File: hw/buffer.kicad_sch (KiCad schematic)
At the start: 35 parts, among them J2001 BNC, J2002 RFShield_Front, J2003 RFShield_Back, K2001 G6L-1F, U2001 TS5A63157DCK, U2002 AQY280S, U2003 AD8370, U2004 OPA859xDSG

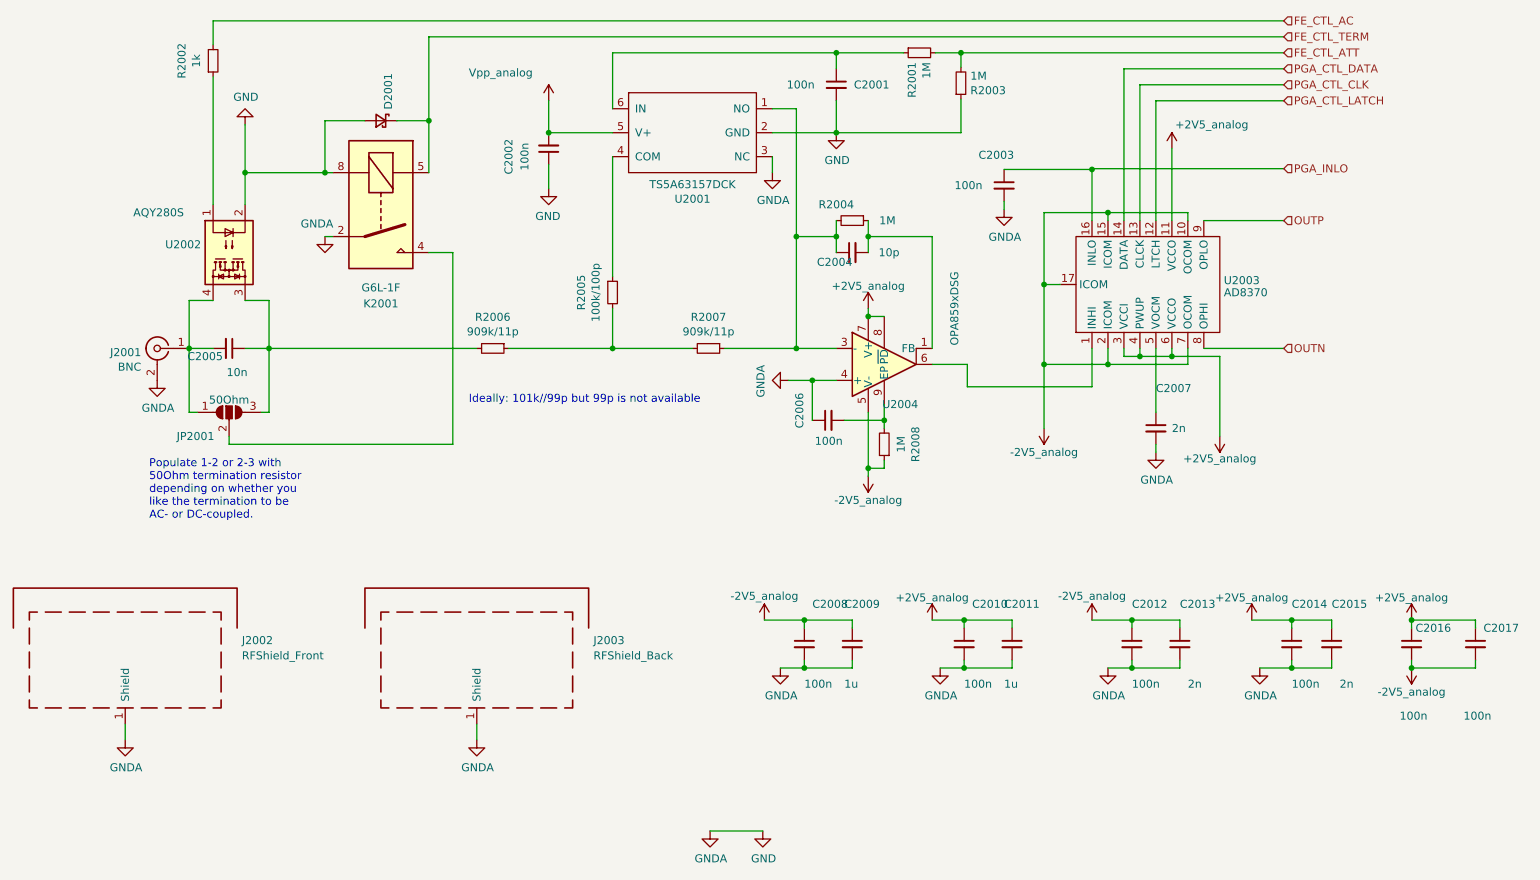
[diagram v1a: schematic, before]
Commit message: added pll clock in divider from BNC, several pull-resistors
pull-resistors permit distinguishing board revisions.
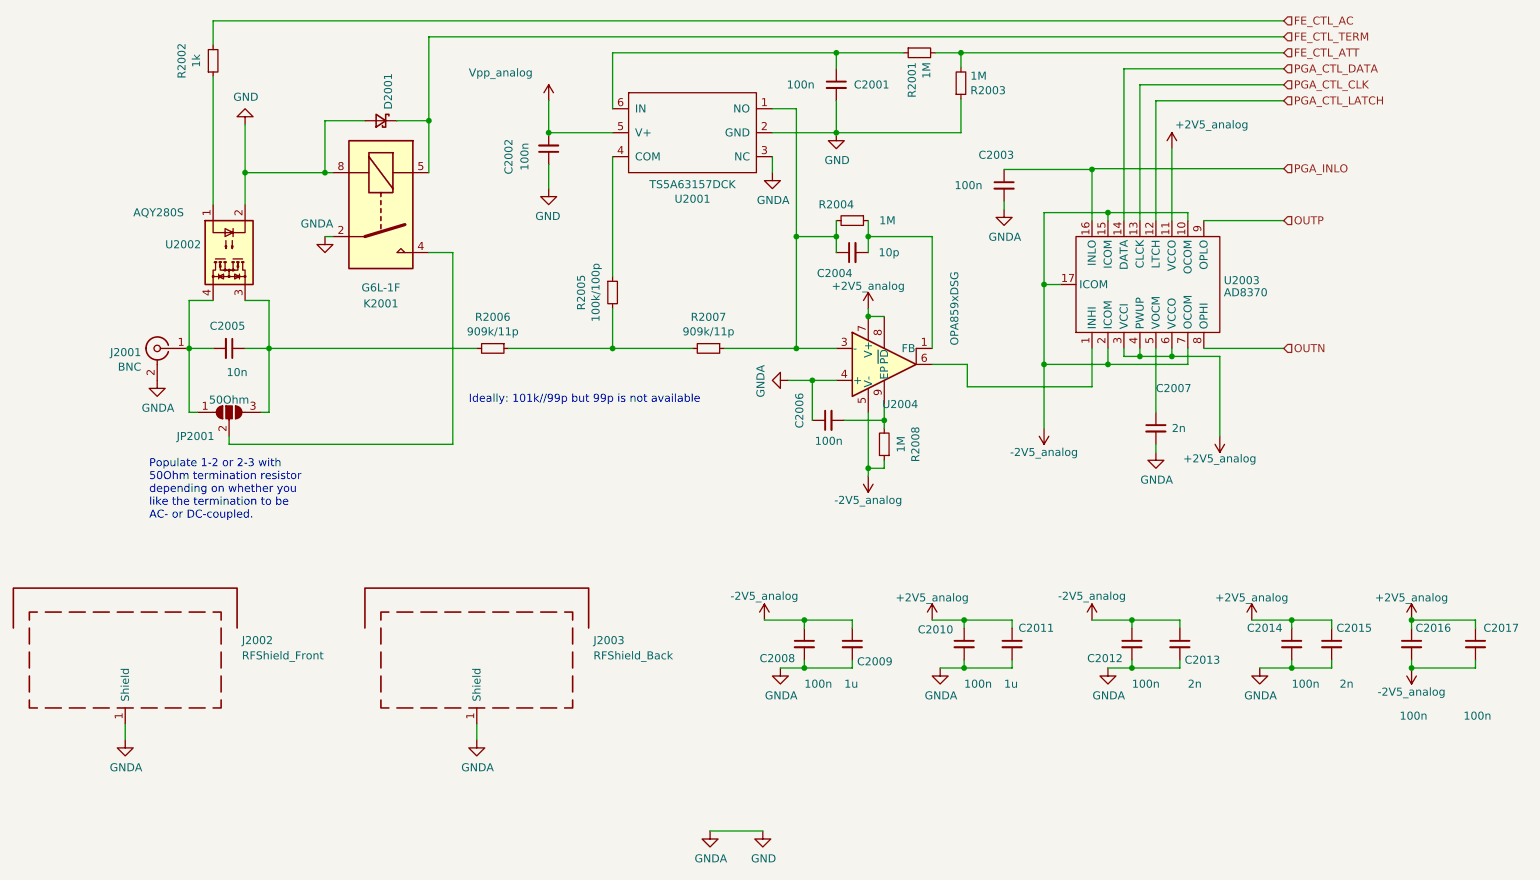
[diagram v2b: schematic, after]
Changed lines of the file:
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@@
 		(dnp no)
 		(property "Reference" "C2010"
-			(at 184.15 142.24 0)
+			(at 175.514 146.304 0)
 			(effects
 				(font
@@
 		(dnp no)
 		(property "Reference" "C2011"
-			(at 189.23 142.24 0)
+			(at 191.516 146.05 0)
 			(effects
 				(font
@@
 		(dnp no)
 		(property "Reference" "C2008"
-			(at 158.75 142.24 0)
+			(at 150.368 150.876 0)
 			(effects
 				(font
@@
 		(dnp no)
 		(property "Reference" "C2009"
-			(at 163.83 142.24 0)
+			(at 165.862 151.384 0)
 			(effects
 				(font
@@
 		(dnp no)
 		(property "Reference" "C2004"
-			(at 162.306 87.884 90)
+			(at 162.306 89.662 90)
 			(effects
 				(font
@@
 		(dnp no)
 		(property "Reference" "C2013"
-			(at 217.17 142.24 0)
+			(at 217.932 151.13 0)
 			(effects
 				(font
@@
 		(dnp no)
 		(property "Reference" "C2015"
-			(at 241.3 142.24 0)
+			(at 242.062 146.05 0)
 			(effects
 				(font
@@
 		(dnp no)
 		(property "Reference" "C2005"
-			(at 62.23 102.87 90)
+			(at 65.786 98.044 90)
 			(effects
 				(font
@@
 		(dnp no)
 		(property "Reference" "C2014"
-			(at 234.95 142.24 0)
+			(at 227.838 146.05 0)
 			(effects
 				(font
@@
 		(dnp no)
 		(property "Reference" "C2012"
-			(at 209.55 142.24 0)
+			(at 202.438 150.876 0)
 			(effects
 				(font

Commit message: updated parts assignments
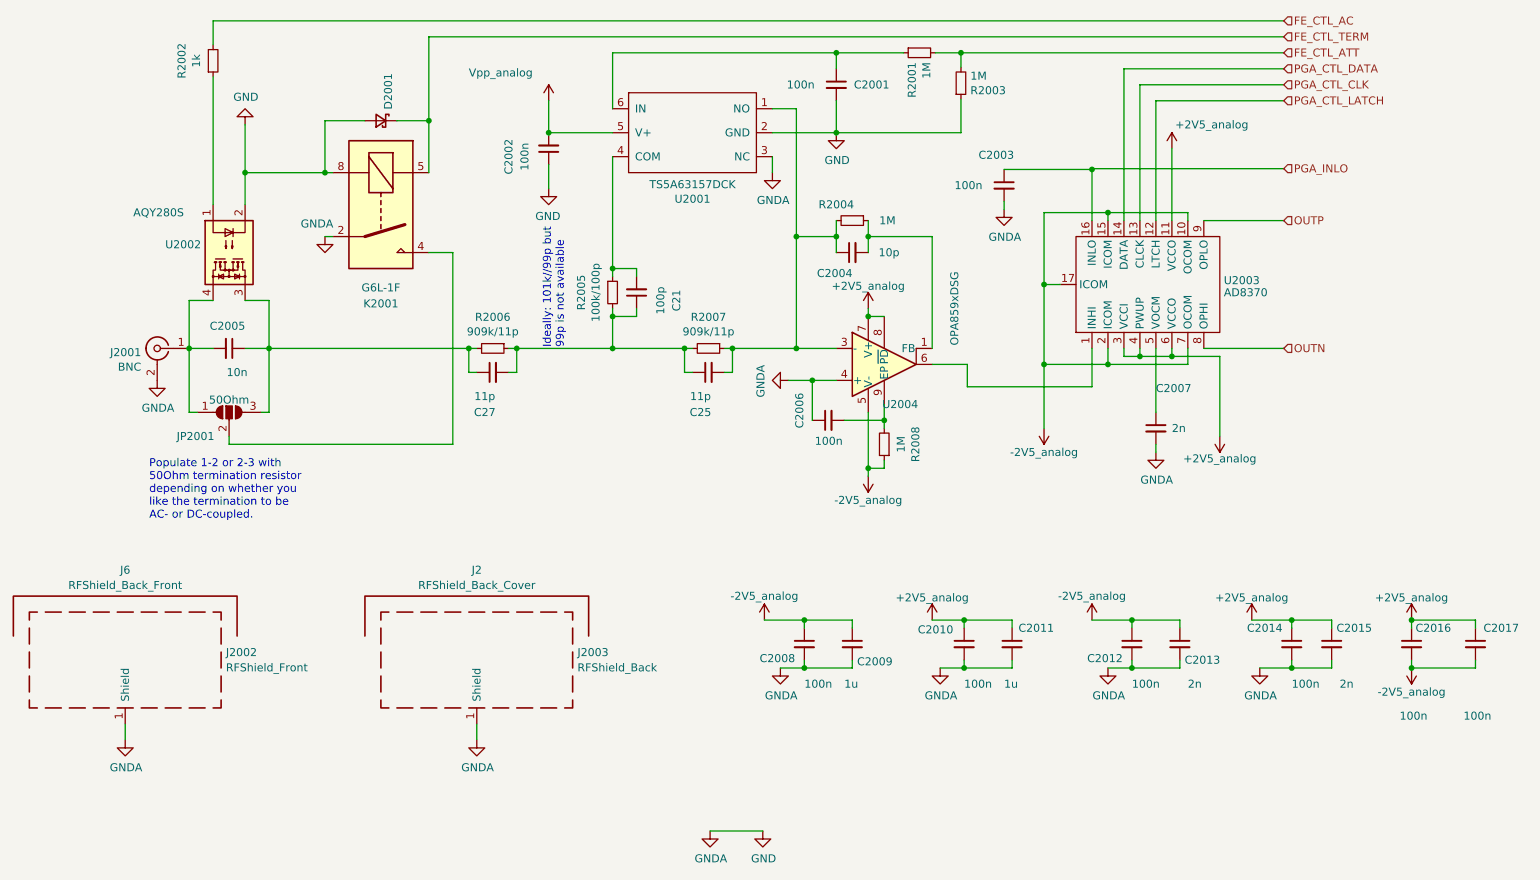
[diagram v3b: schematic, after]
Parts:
- added C21: 100p, Capacitor_SMD:C_0603_1608Metric, symbol Device:C_Small
- added C25, C27: 11p, Capacitor_SMD:C_0603_1608Metric, symbol Device:C_Small
- added J2: RFShield_Back_Cover, symbol fmc:RFShield_Cover
- added J6: RFShield_Back_Front, symbol fmc:RFShield_Cover
- C2004: Manufacturer (none) -> Murata; Part (none) -> GJM1555C1H100FB01D
- C2005: Manufacturer (none) -> Murata; Part (none) -> GRM21B5C2E103JWAAL
- C2007, C2013, C2015: Manufacturer (none) -> Yageo; Part (none) -> CC0603KRX7R9BB202
- J2002: symbol Device:RFShield_TwoPieces -> Device:RFShield_OnePiece; Part SMS-255F+C -> SMS-255F
- J2003: symbol Device:RFShield_TwoPieces -> Device:RFShield_OnePiece; Part SMS-202F+C -> SMS-202F
- JP2001: Manufacturer (none) -> Panasonic; Part (none) -> ERJ-PA3F49R9V
- R2001, R2003, R2008: Manufacturer (none) -> Stackpole; Part (none) -> RMCF0603FT1M00
- R2002: Manufacturer (none) -> Stackpole; Part (none) -> RMCF0603FT1K00
- R2004: Manufacturer (none) -> Stackpole; Part (none) -> RMCF0402FT1M00
- R2005: Manufacturer (none) -> Stackpole; Part (none) -> RMCF0603FT100K
- R2006, R2007: Manufacturer (none) -> Panasonic; Part (none) -> ERJ-3EKF9093V
- U2001: Manufacturer (none) -> TI; Part (none) -> TS5A63157DCKR
- U2002: Manufacturer (none) -> Panasonic; Part (none) -> AQY280S
- U2003: Manufacturer (none) -> AD; Part (none) -> AD8370AREZ
- U2004: Manufacturer (none) -> TI; Part (none) -> OPA859IDSGR
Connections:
- net at R2005.1, U2001.4 (COM): now also C21.2
- net at R2005.2, R2006.1, R2007.2: now also C21.1, C25.1, C27.2
- net at C2005.1, JP2001.3 (B), R2006.2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: now also C27.1
- net at C2004.1, R2004.2, R2007.1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: now also C25.2

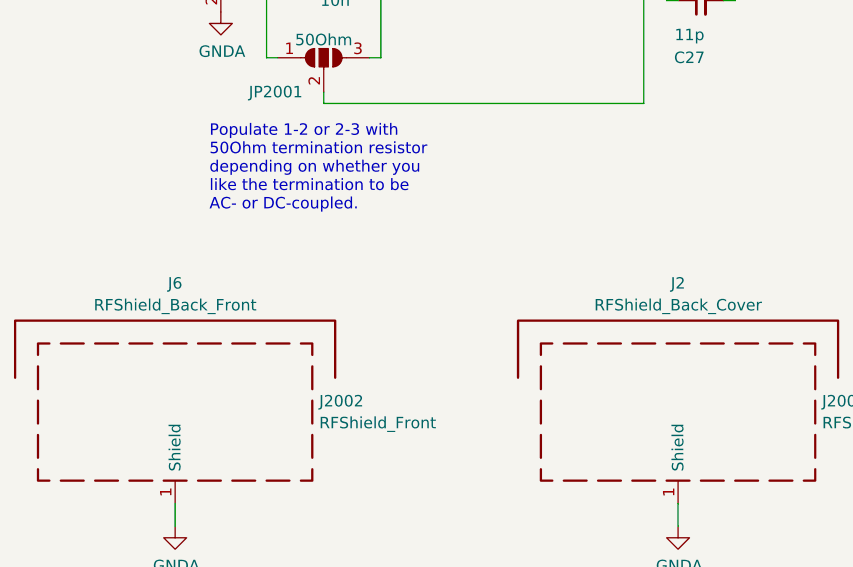
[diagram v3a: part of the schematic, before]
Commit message: fixed BOM; added relay drivers
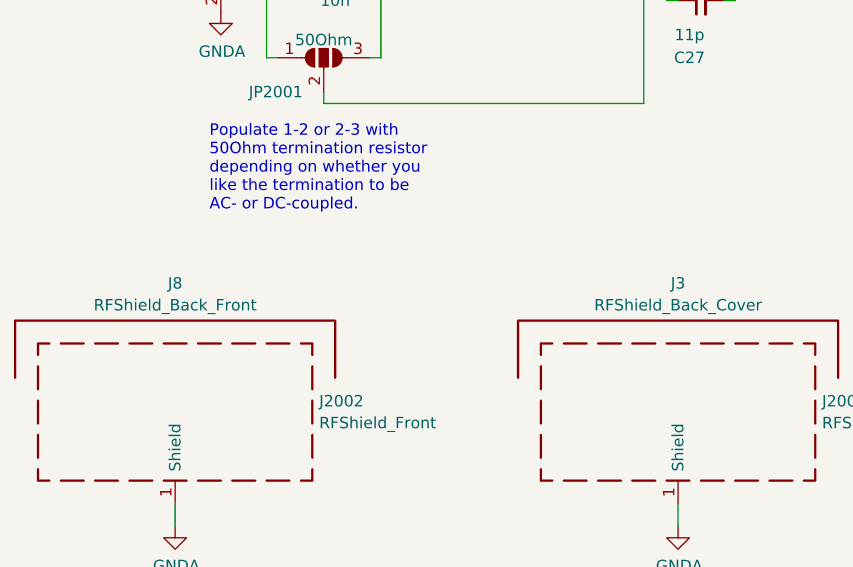
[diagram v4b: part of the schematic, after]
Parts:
- K2001: Part G6L-1F -> G6L-1F DC4.5
- renumbered J2 to J3, J6 to J8
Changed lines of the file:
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@@
 			)
 		)
-		(property "Part" "G6L-1F"
+		(property "Part" "G6L-1F DC4.5"
 			(at 90.17 78.74 90)
 			(effects
@@
 		(dnp no)
 		(fields_autoplaced yes)
-		(property "Reference" "J6"
+		(property "Reference" "J8"
 			(at 49.53 136.8255 0)
 			(effects
@@
 		(dnp no)
 		(fields_autoplaced yes)
-		(property "Reference" "J2"
+		(property "Reference" "J3"
 			(at 105.41 136.8255 0)
 			(effects

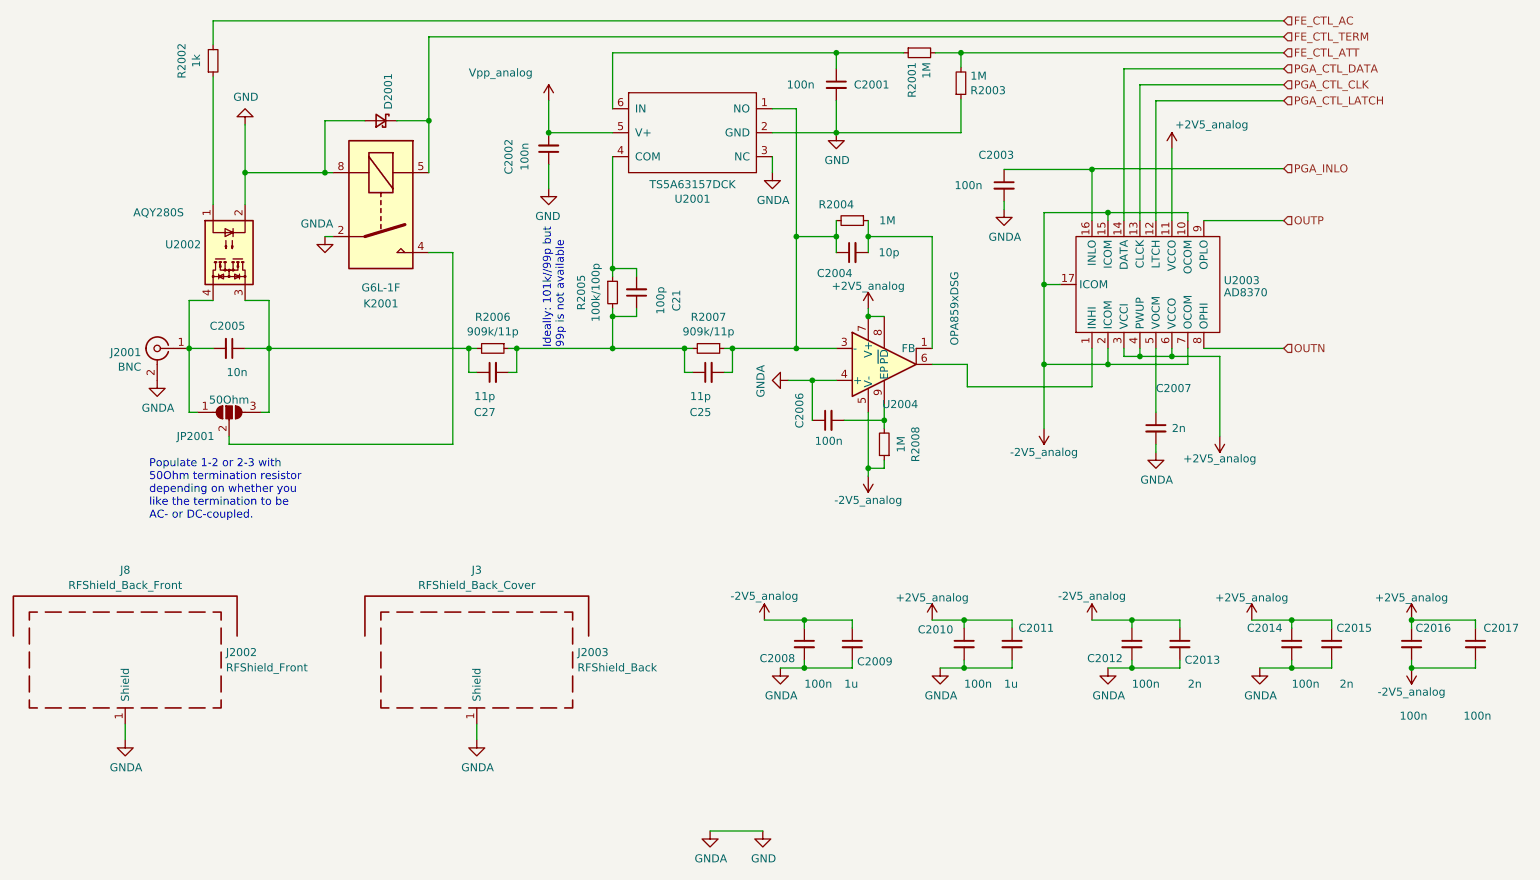
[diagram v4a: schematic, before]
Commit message: connected versaclock CLKSEL to ULPI RSTB (share FPGA pin)
ULPI Rstb is unlikely to be used

Also: - update of kicad to 9.0 (many library footprints updated)
      - added sheet titles, author
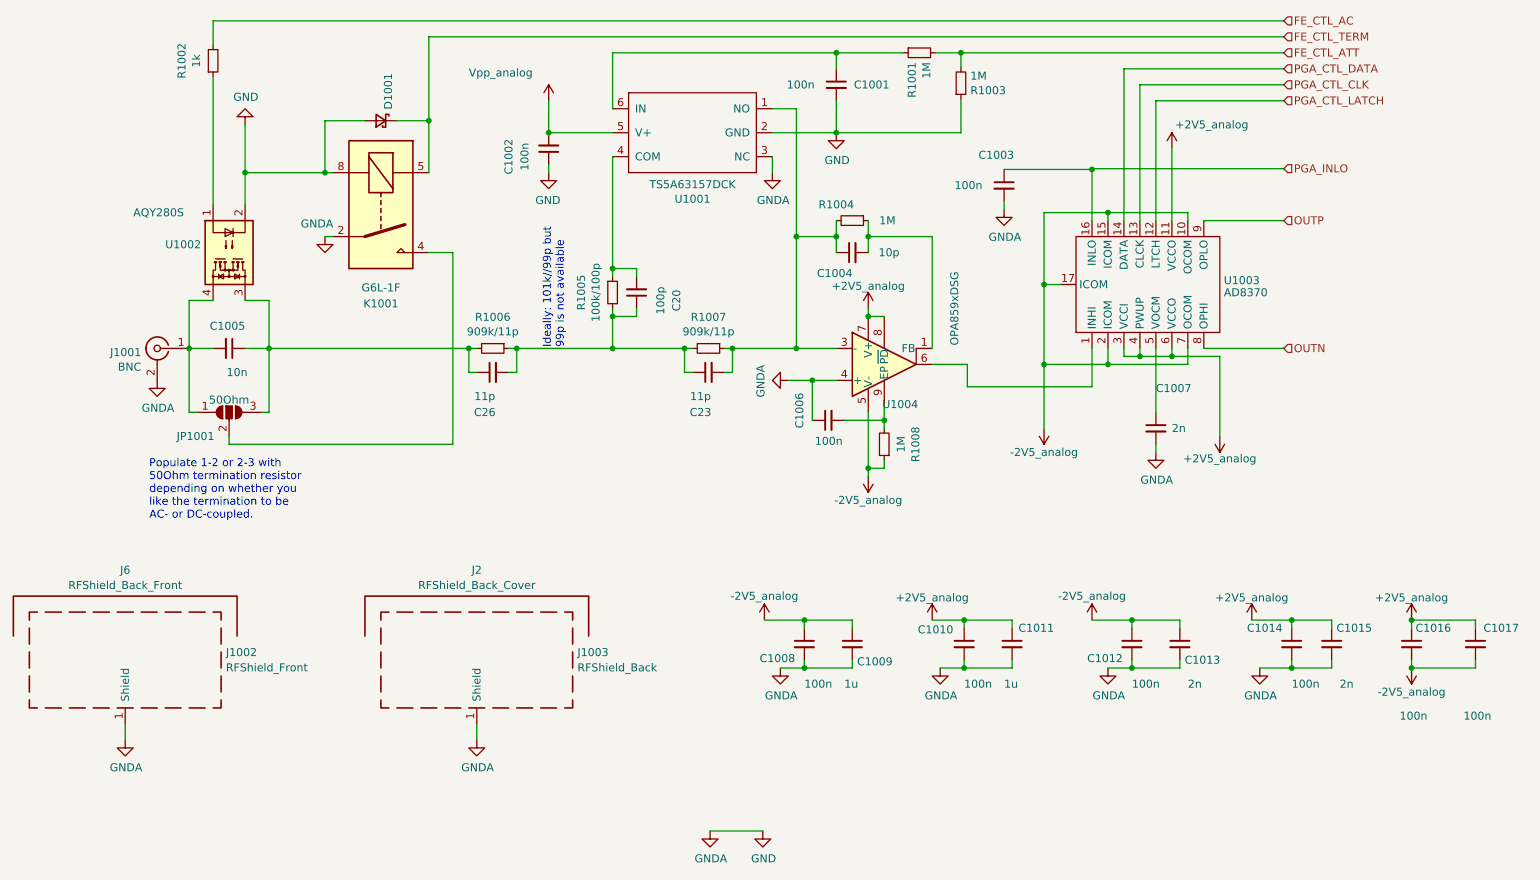
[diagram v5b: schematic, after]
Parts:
- renumbered C2001 to C1001, C2002 to C1002, C2003 to C1003, C2004 to C1004, C2005 to C1005, C2006 to C1006, C2007 to C1007, C2008 to C1008, C2009 to C1009, C2010 to C1010, C2011 to C1011, C2012 to C1012, C2013 to C1013, C2014 to C1014, C2015 to C1015, C2016 to C1016, C2017 to C1017, C21 to C20, C25 to C23, C27 to C26, D2001 to D1001, J2001 to J1001, J2002 to J1002, J2003 to J1003, J3 to J2, J8 to J6, JP2001 to JP1001, K2001 to K1001, R2001 to R1001, R2002 to R1002, R2003 to R1003, R2004 to R1004, R2005 to R1005, R2006 to R1006, R2007 to R1007, R2008 to R1008, U2001 to U1001, U2002 to U1002, U2003 to U1003, U2004 to U1004
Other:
- company: (none) -> Till Straumann
- title: (none) -> Input Stage, Buffer And PGA

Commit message: Added licensing information
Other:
- company: Till Straumann -> Copyright Till Straumann, 2025
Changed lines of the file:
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@@
 		(title "Input Stage, Buffer And PGA")
 		(rev "3.3b")
-		(company "Till Straumann")
+		(company "Copyright Till Straumann, 2025")
+		(comment 1 "License: CERN-OHL-P v2")
 	)
 	(text "Ideally: 101k//99p but\n99p is not available"
